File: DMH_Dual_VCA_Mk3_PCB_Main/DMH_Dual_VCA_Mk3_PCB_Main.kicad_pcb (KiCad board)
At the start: 2 copper layers, 49 x 121 mm, 98 parts, among them J10 Conn_01x04, J11 Conn_01x04_PinHeader, J50 Conn_01x08, J60 Conn_01x08, Q5 BC548, Q6 BC548, Q7 BC548, Q8 BC548, SW1 SW_DPDT_OnOffOn_x2, SW2 SW_DPDT_3way, U3 TL074, U4 TL072, U7 TL074, U8 TL074

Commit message: Started Main PCB comp placement
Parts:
- removed C11: 22pF, Capacitor_THT:C_Disc_D3.0mm_W2.0mm_P2.50mm
- removed C12, C13, C14, C15, C16, C17: 100nF, Capacitor_THT:C_Disc_D4.3mm_W1.9mm_P5.00mm
- removed D10, D9: ZPD3V0, Diode_THT:D_DO-35_SOD27_P7.62mm_Horizontal
- removed D5, D6, D7, D8: ZPD4V7, Diode_THT:D_DO-35_SOD27_P7.62mm_Horizontal
- removed J10: Conn_01x04, Connector_PinSocket_2.54mm:PinSocket_1x04_P2.54mm_Vertical
- removed J50, J60: Conn_01x08, Connector_PinSocket_2.54mm:PinSocket_1x08_P2.54mm_Vertical
- removed Q5, Q6, Q7, Q8: BC548, Package_TO_SOT_THT:TO-92L_Inline_Wide
- removed R20: 2k2, Resistor_THT:R_Axial_DIN0207_L6.3mm_D2.5mm_P7.62mm_Horizontal
- removed R21, R40: 18k, Resistor_THT:R_Axial_DIN0207_L6.3mm_D2.5mm_P7.62mm_Horizontal
- removed R27, R29, R37, R50, R51, R52, R53, R54, R55, R56, R64, R65, R66, R67, R69, R70, R71, R72, R74, R75: 100k, Resistor_THT:R_Axial_DIN0207_L6.3mm_D2.5mm_P7.62mm_Horizontal
- removed R43, R47, R57, R63: 100R, Resistor_THT:R_Axial_DIN0207_L6.3mm_D2.5mm_P7.62mm_Horizontal
- removed R44, R46, R58, R60: 20k, Resistor_THT:R_Axial_DIN0207_L6.3mm_D2.5mm_P7.62mm_Horizontal
- removed R45, R48, R49, R59, R61, R62: 10k, Resistor_THT:R_Axial_DIN0207_L6.3mm_D2.5mm_P7.62mm_Horizontal
- removed R68: 33k, Resistor_THT:R_Axial_DIN0207_L6.3mm_D2.5mm_P7.62mm_Horizontal
- removed RV13: 50k, Potentiometer_THT:Potentiometer_Alps_RK09L_Double_Vertical
- removed RV14, RV15: 100k, Potentiometer_THT:Potentiometer_Bourns_3296W_Vertical
- removed RV16: 50k, Potentiometer_THT:Potentiometer_Bourns_3296W_Vertical
- removed RV2, RV3, RV5, RV6: 100k, SynthStuff:Potentiometer_TT_P110KH1
- removed RV4: 100k, SynthStuff:Potentiometer_Alpha_RD901F-40-00D_Single_Vertical
- removed SW1: SW_DPDT_OnOffOn_x2, SynthStuff:Toggle_Switch_2_Poles_TE
- removed SW2: SW_DPDT_3way, SynthStuff:Toggle_Switch_2_Poles_TE
- removed U7, U8: TL074, Package_DIP:DIP-14_W7.62mm_Socket
- added C1: 100nF, Capacitor_THT:C_Disc_D4.3mm_W1.9mm_P5.00mm, B.Cu at (160.8, 77.0)
- added C2: 100nF, Capacitor_THT:C_Disc_D4.3mm_W1.9mm_P5.00mm, B.Cu at (160.8, 80.5)
- added C20: 2.2uF, Capacitor_THT:CP_Radial_D4.0mm_P1.50mm, B.Cu at (139.1, 184.9)
- added C21: 2.2uF, Capacitor_THT:CP_Radial_D4.0mm_P1.50mm, B.Cu at (139.1, 190.4)
- added C22: 22uF, Capacitor_THT:CP_Radial_D4.0mm_P1.50mm, B.Cu at (139.1, 196.0)
- added C23: 22uF, Capacitor_THT:CP_Radial_D4.0mm_P1.50mm, B.Cu at (139.1, 201.6)
- added C24: 100nF, Capacitor_THT:C_Disc_D4.3mm_W1.9mm_P5.00mm, B.Cu at (160.8, 97.8)
- added C25: 100nF, Capacitor_THT:C_Disc_D4.3mm_W1.9mm_P5.00mm, B.Cu at (160.8, 101.2)
- added C3: 22pF, Capacitor_THT:C_Disc_D3.0mm_W2.0mm_P2.50mm, B.Cu at (146.1, 216.5)
- added C4: 47uF, Capacitor_THT:CP_Radial_D5.0mm_P2.00mm, B.Cu at (55.2, 47.0)
- added C5: 47uF, Capacitor_THT:CP_Radial_D5.0mm_P2.00mm, B.Cu at (94.8, 45.0)
- added C6: 100nF, Capacitor_THT:C_Disc_D4.3mm_W1.9mm_P5.00mm, B.Cu at (160.8, 84.0)
- added C9: 100nF, Capacitor_THT:C_Disc_D4.3mm_W1.9mm_P5.00mm, B.Cu at (160.8, 94.3)
- added D1: 1N4148, Diode_THT:D_DO-35_SOD27_P7.62mm_Horizontal, B.Cu at (156.5, 164.5)
- added D13: ZPD3V0, Diode_THT:D_DO-35_SOD27_P7.62mm_Horizontal, B.Cu at (139.6, 160.8)
- added D14: ZPD3V0, Diode_THT:D_DO-35_SOD27_P7.62mm_Horizontal, B.Cu at (139.6, 164.3)
- added D2: 1N4148, Diode_THT:D_DO-35_SOD27_P7.62mm_Horizontal, B.Cu at (156.5, 170.7)
- added J1: TRS_Jack_6.35mm_Sw, SynthStuff:CUI_SJ-63083D, F.Cu at (58.5, 190.2)
- added J100: IDC_02x05, SynthStuff:IDC-Header_2x05_P2.54mm_Vertical_Eurorack, B.Cu at (80.1, 48.8)
- added J12: Conn_01x08, Connector_PinHeader_2.54mm:PinHeader_1x08_P2.54mm_Vertical, F.Cu at (97.2, 138.9)
- added J13: Conn_01x06, Connector_PinHeader_2.54mm:PinHeader_1x06_P2.54mm_Vertical, F.Cu at (52.8, 52.0)
- added J18: Conn_02x03_Odd_Even, Connector_PinSocket_2.54mm:PinSocket_2x03_P2.54mm_Vertical, B.Cu at (171.2, 114.4)
- added J19: Conn_02x03_Odd_Even, Connector_PinSocket_2.54mm:PinSocket_2x03_P2.54mm_Vertical, B.Cu at (171.2, 124.1)
- added J2: TRS_Jack_6.35mm_Sw, SynthStuff:CUI_SJ-63083D, F.Cu at (75.0, 190.2)
- added J20: Conn_01x01, Connector_PinHeader_2.54mm:PinHeader_1x01_P2.54mm_Vertical, B.Cu at (40.2, 46.2)
- added J200: IDC_02x05, SynthStuff:IDC-Header_2x05_P2.54mm_Vertical_BackBone, B.Cu at (71.4, 157.2)
- added J21: Conn_01x08, Connector_PinHeader_2.54mm:PinHeader_1x08_P2.54mm_Vertical, F.Cu at (97.2, 52.0)
- added J22: Conn_02x03_Odd_Even, Connector_PinSocket_2.54mm:PinSocket_2x03_P2.54mm_Vertical, B.Cu at (171.2, 133.8)
- added J23: Conn_02x03_Odd_Even, Connector_PinSocket_2.54mm:PinSocket_2x03_P2.54mm_Vertical, B.Cu at (171.2, 143.5)
- added J3: TRS_Jack_6.35mm_Sw, SynthStuff:CUI_SJ-63083D, F.Cu at (58.5, 171.8)
- added J4: TRS_Jack_6.35mm_Sw, SynthStuff:CUI_SJ-63083D, F.Cu at (91.5, 190.2)
- added J5: TRS_Jack_6.35mm_Sw, SynthStuff:CUI_SJ-63083D, F.Cu at (58.5, 208.8)
- added J6: TRS_Jack_6.35mm_Sw, SynthStuff:CUI_SJ-63083D, F.Cu at (75.0, 208.8)
- added J7: TRS_Jack_6.35mm_Sw, SynthStuff:CUI_SJ-63083D, F.Cu at (75.0, 171.8)
- added J8: TRS_Jack_6.35mm_Sw, SynthStuff:CUI_SJ-63083D, F.Cu at (91.5, 208.8)
- added J9: TRS_Jack_6.35mm_Sw, SynthStuff:CUI_SJ-63083D, F.Cu at (91.5, 171.8)
- added JP1: Jumper, Connector_PinHeader_2.54mm:PinHeader_1x03_P2.54mm_Vertical, B.Cu at (90.5, 160.5)
- added Q10: BC548, Package_TO_SOT_THT:TO-92_Inline, B.Cu at (150.3, 191.2)
- added Q11: BC548, Package_TO_SOT_THT:TO-92_Inline, B.Cu at (150.3, 197.0)
- added Q12: BC548, Package_TO_SOT_THT:TO-92_Inline, B.Cu at (150.3, 202.8)
- added Q9: BC548, Package_TO_SOT_THT:TO-92_Inline, B.Cu at (150.3, 185.4)
- added R1: 3k3, Resistor_THT:R_Axial_DIN0207_L6.3mm_D2.5mm_P7.62mm_Horizontal, B.Cu at (151.8, 77.3)
- added R10: 10k, Resistor_THT:R_Axial_DIN0207_L6.3mm_D2.5mm_P7.62mm_Horizontal, B.Cu at (151.8, 113.8)
- added R100: 1k, Resistor_THT:R_Axial_DIN0207_L6.3mm_D2.5mm_P7.62mm_Horizontal, B.Cu at (118.1, 101.6)
- added R101: 1k, Resistor_THT:R_Axial_DIN0207_L6.3mm_D2.5mm_P7.62mm_Horizontal, B.Cu at (118.1, 105.7)
- added R11: 20k, Resistor_THT:R_Axial_DIN0207_L6.3mm_D2.5mm_P7.62mm_Horizontal, B.Cu at (151.8, 117.8)
- added R12: 100k, Resistor_THT:R_Axial_DIN0207_L6.3mm_D2.5mm_P7.62mm_Horizontal, B.Cu at (151.8, 121.9)
- added R13: 100k, Resistor_THT:R_Axial_DIN0207_L6.3mm_D2.5mm_P7.62mm_Horizontal, B.Cu at (151.8, 125.9)
- added R14: 100k, Resistor_THT:R_Axial_DIN0207_L6.3mm_D2.5mm_P7.62mm_Horizontal, B.Cu at (151.8, 130.0)
- added R15: 100k, Resistor_THT:R_Axial_DIN0207_L6.3mm_D2.5mm_P7.62mm_Horizontal, B.Cu at (151.8, 134.0)
- added R2: 3k3, Resistor_THT:R_Axial_DIN0207_L6.3mm_D2.5mm_P7.62mm_Horizontal, B.Cu at (151.8, 81.4)
- added R3: 33k, Resistor_THT:R_Axial_DIN0207_L6.3mm_D2.5mm_P7.62mm_Horizontal, B.Cu at (151.8, 85.4)
- added R4: 100k, Resistor_THT:R_Axial_DIN0207_L6.3mm_D2.5mm_P7.62mm_Horizontal, B.Cu at (151.8, 89.5)
- added R6: 100k, Resistor_THT:R_Axial_DIN0207_L6.3mm_D2.5mm_P7.62mm_Horizontal, B.Cu at (151.8, 97.6)
- added R7: 100k, Resistor_THT:R_Axial_DIN0207_L6.3mm_D2.5mm_P7.62mm_Horizontal, B.Cu at (151.8, 101.6)
- added R8: 100k, Resistor_THT:R_Axial_DIN0207_L6.3mm_D2.5mm_P7.62mm_Horizontal, B.Cu at (151.8, 105.7)
- added R9: 20k, Resistor_THT:R_Axial_DIN0207_L6.3mm_D2.5mm_P7.62mm_Horizontal, B.Cu at (151.8, 109.7)
- added R92: 100k, Resistor_THT:R_Axial_DIN0207_L6.3mm_D2.5mm_P7.62mm_Horizontal, B.Cu at (128.9, 105.7)
- added R93: 100k, Resistor_THT:R_Axial_DIN0207_L6.3mm_D2.5mm_P7.62mm_Horizontal, B.Cu at (128.9, 109.7)
- added R94: 220k, Resistor_THT:R_Axial_DIN0207_L6.3mm_D2.5mm_P7.62mm_Horizontal, B.Cu at (118.1, 77.3)
- added R95: 220k, Resistor_THT:R_Axial_DIN0207_L6.3mm_D2.5mm_P7.62mm_Horizontal, B.Cu at (118.1, 81.3)
- added R96: 100k, Resistor_THT:R_Axial_DIN0207_L6.3mm_D2.5mm_P7.62mm_Horizontal, B.Cu at (118.1, 85.4)
- added R97: 100k, Resistor_THT:R_Axial_DIN0207_L6.3mm_D2.5mm_P7.62mm_Horizontal, B.Cu at (118.1, 89.5)
- added R98: 2k2, Resistor_THT:R_Axial_DIN0207_L6.3mm_D2.5mm_P7.62mm_Horizontal, B.Cu at (118.1, 93.5)
- added R99: 2k2, Resistor_THT:R_Axial_DIN0207_L6.3mm_D2.5mm_P7.62mm_Horizontal, B.Cu at (118.1, 97.5)
- added U1: LM4040LP-5, Package_TO_SOT_THT:TO-92_Inline, B.Cu at (155.6, 148.2)
- added U10: TL074, Package_DIP:DIP-14_W7.62mm_Socket, B.Cu at (121.7, 126.7)
- added U2: LM4040LP-5, Package_TO_SOT_THT:TO-92_Inline, B.Cu at (155.6, 156.4)
- C7, C8, D11, D12, R5, R80, R81, R83, R87, U3, U4: moved to B.Cu
- D3, D4: value 1N4148 -> SB140; footprint Diode_THT:D_DO-35_SOD27_P7.62mm_Horizontal -> Diode_THT:D_DO-41_SOD81_P10.16mm_Horizontal; moved to B.Cu
- J11: value Conn_01x04_PinHeader -> Conn_01x06; footprint Connector_PinSocket_2.54mm:PinSocket_1x04_P2.54mm_Vertical -> Connector_PinHeader_2.54mm:PinHeader_1x06_P2.54mm_Vertical
- R76: value 100k -> 10k; moved to B.Cu
- R77: value 20k -> 1k5; moved to B.Cu
- R78: value 20k -> 10k; moved to B.Cu
- R79: value 10k -> 1k5; moved to B.Cu
- R82: value 220k -> 100k; moved to B.Cu
- R84: value 2k2 -> 100k; moved to B.Cu
- R85: value 100k -> 4k7; moved to B.Cu
- R86: value 220k -> 1k; moved to B.Cu
- R88: value 2k2 -> 4k7; moved to B.Cu
- R89: value 2k2 -> 1k; moved to B.Cu
- R90, R91: value 1k -> 2k2; moved to B.Cu
- RV1: value 100k -> 50k; footprint SynthStuff:Potentiometer_Alpha_RD901F-40-00D_Single_Vertical -> Potentiometer_THT:Potentiometer_Bourns_3296W_Vertical; moved to B.Cu
- moved J11 179.2 mm to (52.8, 144.0)
- moved RV1 174.3 mm to (142.2, 228.0), turned to 180 degrees
- moved D4 151.9 mm to (61.2, 54.6), turned to 90 degrees
- moved D3 136.0 mm to (88.8, 44.4), turned to -90 degrees
- moved R85 81.8 mm to (128.9, 77.3), turned to 180 degrees
- moved R86 81.8 mm to (128.9, 81.3), turned to 180 degrees
- moved R87 81.8 mm to (128.9, 85.4), turned to 180 degrees
- moved R88 81.8 mm to (128.9, 89.5), turned to 180 degrees
- moved R89 81.8 mm to (128.9, 93.5), turned to 180 degrees
- moved R90 81.8 mm to (128.9, 97.5), turned to 180 degrees
- moved R91 81.8 mm to (128.9, 101.6), turned to 180 degrees
- moved D11 81.0 mm to (139.6, 153.7), turned to 180 degrees
- moved D12 81.0 mm to (139.6, 157.2), turned to 180 degrees
- moved C7 68.8 mm to (160.8, 87.4), turned to 180 degrees
- moved C8 68.8 mm to (160.8, 90.8), turned to 180 degrees
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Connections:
- C7 pad 1: +12V -> GND
- C7 pad 2: GND -> -12V
- C8 pad 1: GND -> +12V
- C8 pad 2: -12V -> GND
- D11 pad 1: Net-(D11-K) -> /Clipping/Clip_Sw_p1_m
- D3 pad 2: Net-(D3-A) -> -12V
- D4 pad 1: Net-(D4-K) -> +12V
- D4 pad 2: Net-(D3-K) -> Net-(D4-A)
- J11 pad 1: /2nd VCA/Input A -> /Processed_CV_A_m
- J11 pad 2: /Clipping/Output A -> /Processed_CV_B_m
- J11 pad 3: /Clipping/Output B -> /CV_In_A1_m
- J11 pad 4: /2nd VCA/Input B -> /CV_In_A2_m
- R5 pad 1: /2nd VCA/CV PT Offset -> Net-(D2-K)
- R5 pad 2: Net-(U3A--) -> GND
- R76 pad 1: Net-(D4-K) -> Net-(Q9-B)
- R76 pad 2: GND -> Net-(C20-Pad2)
- R77 pad 1: Net-(U7C--) -> -12V
- R77 pad 2: Net-(R75-Pad1) -> Net-(Q9-B)
- R78 pad 1: /2nd VCA/Balanced Offset -> Net-(Q10-B)
- R78 pad 2: Net-(U7C--) -> Net-(C21-Pad2)
- R79 pad 1: -5V -> -12V
- R79 pad 2: Net-(U7C--) -> Net-(Q10-B)
- R80 pad 1: Net-(U8B--) -> /Clip_In_A_m
- R80 pad 2: Net-(R80-Pad2) -> Net-(U10A--)
- R81 pad 1: Net-(SW1A-B) -> /Clip_In_B_m
- R81 pad 2: Net-(U8B--) -> Net-(U10D--)
- R82 pad 2: Net-(U8B--) -> +12V
- R83 pad 1: Net-(R83-Pad1) -> Net-(Q10-C)
- R83 pad 2: Net-(U8D--) -> +12V
- R84 pad 1: Net-(R83-Pad1) -> Net-(R84-Pad1)
- R84 pad 2: Net-(SW1B-B) -> Net-(U10A--)
- R85 pad 1: Net-(SW1B-B) -> /Clipping/LED_A_pA_m
- R85 pad 2: Net-(U8C--) -> +12V
- R86 pad 1: Net-(D11-K) -> -12V
- R86 pad 2: Net-(U8C--) -> /Clipping/LED_A_pK_m
- R87 pad 1: Net-(U8C--) -> Net-(R87-Pad1)
- R87 pad 2: Net-(R87-Pad2) -> Net-(U10D--)
- R88 pad 1: Net-(R80-Pad2) -> /Clipping/LED_B_pA_m
- R88 pad 2: Net-(R88-Pad2) -> +12V
- R89 pad 1: Net-(R87-Pad2) -> -12V
- R89 pad 2: Net-(R89-Pad2) -> /Clipping/LED_B_pK_m
- R90 pad 1: Net-(R88-Pad2) -> Net-(R84-Pad1)
- R90 pad 2: /Clipping/Output A -> /Clipping/Clip_Sw_p2_m
- R91 pad 1: Net-(R89-Pad2) -> Net-(R87-Pad1)
- R91 pad 2: /Clipping/Output B -> /Clipping/Clip_Sw_p5_m
- RV1 pad 1: GND -> Net-(U4A--)
- RV1 pad 2: /Inputs and Outputs/Offset A Pot -> /Attenuverted_CV_PT_m
- RV1 pad 3: Net-(R21-Pad1) -> /Attenuverted_CV_PT_m
- U3 pad 10: Net-(U3C-+) -> GND
- U3 pad 14: Net-(R45-Pad1) -> Net-(U3D--)
- U3 pad 2: Net-(U3A--) -> Net-(D1-A)
- U3 pad 3: GND -> /CV_PT_Pot_G2_m
- U3 pad 5: Net-(U3B-+) -> Net-(D2-K)
- U3 pad 7: /2nd VCA/Output B -> Net-(R7-Pad1)
- U3 pad 8: /2nd VCA/Output A -> /Balanced_Offset_m
- U4 pad 1: /2nd VCA/Attenuverted CV PT -> /Attenuverted_CV_PT_m
- U4 pad 3: /2nd VCA/CV PT Pot G1 -> /CV_PT_Pot_G1_m
- U4 pad 7: /2nd VCA/Inverted CV PT -> /Inverted_CV_PT_m
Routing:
- added copper zone on B.Cu, net GND
- added copper zone on F.Cu, net GND
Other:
- board size 49 x 121 mm -> 49 x 175 mm
- board text added: "Mk3.0 June 2026"
- board text removed: "Mk2.0 - October 2025"

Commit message: Comp placement in progress
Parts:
- moved J22 101.5 mm to (73.0, 108.0), turned to 90 degrees
- moved J19 101.0 mm to (73.0, 147.6), turned to 90 degrees
- moved J23 100.7 mm to (73.0, 121.2), turned to 90 degrees
- moved J18 100.2 mm to (73.0, 134.4), turned to 90 degrees
- moved U3 95.3 mm to (68.5, 83.8)
- moved C8 94.2 mm to (67.2, 80.6)
- moved C9 93.8 mm to (67.4, 102.7)
- moved C24 91.9 mm to (77.5, 59.1)
- moved C25 85.8 mm to (77.5, 80.9)
- moved U10 77.3 mm to (78.8, 62.4)
- moved U4 65.8 mm to (89.3, 91.5)
- moved R100 6.50 mm to (111.6, 101.8)
- moved J200 1.50 mm to (69.9, 157.3)
- moved JP1 1.50 mm to (89.0, 160.6)
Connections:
- J200 pad 1: /Input_A_N_m -> /CV_In_A2_N_m
- J200 pad 3: /CV_In_A1_N_m -> /CV_In_B2_N_m
- J200 pad 6: /CV_In_A2_N_m -> /Input_A_N_m
- J200 pad 8: /CV_In_B2_N_m -> /CV_In_A1_N_m

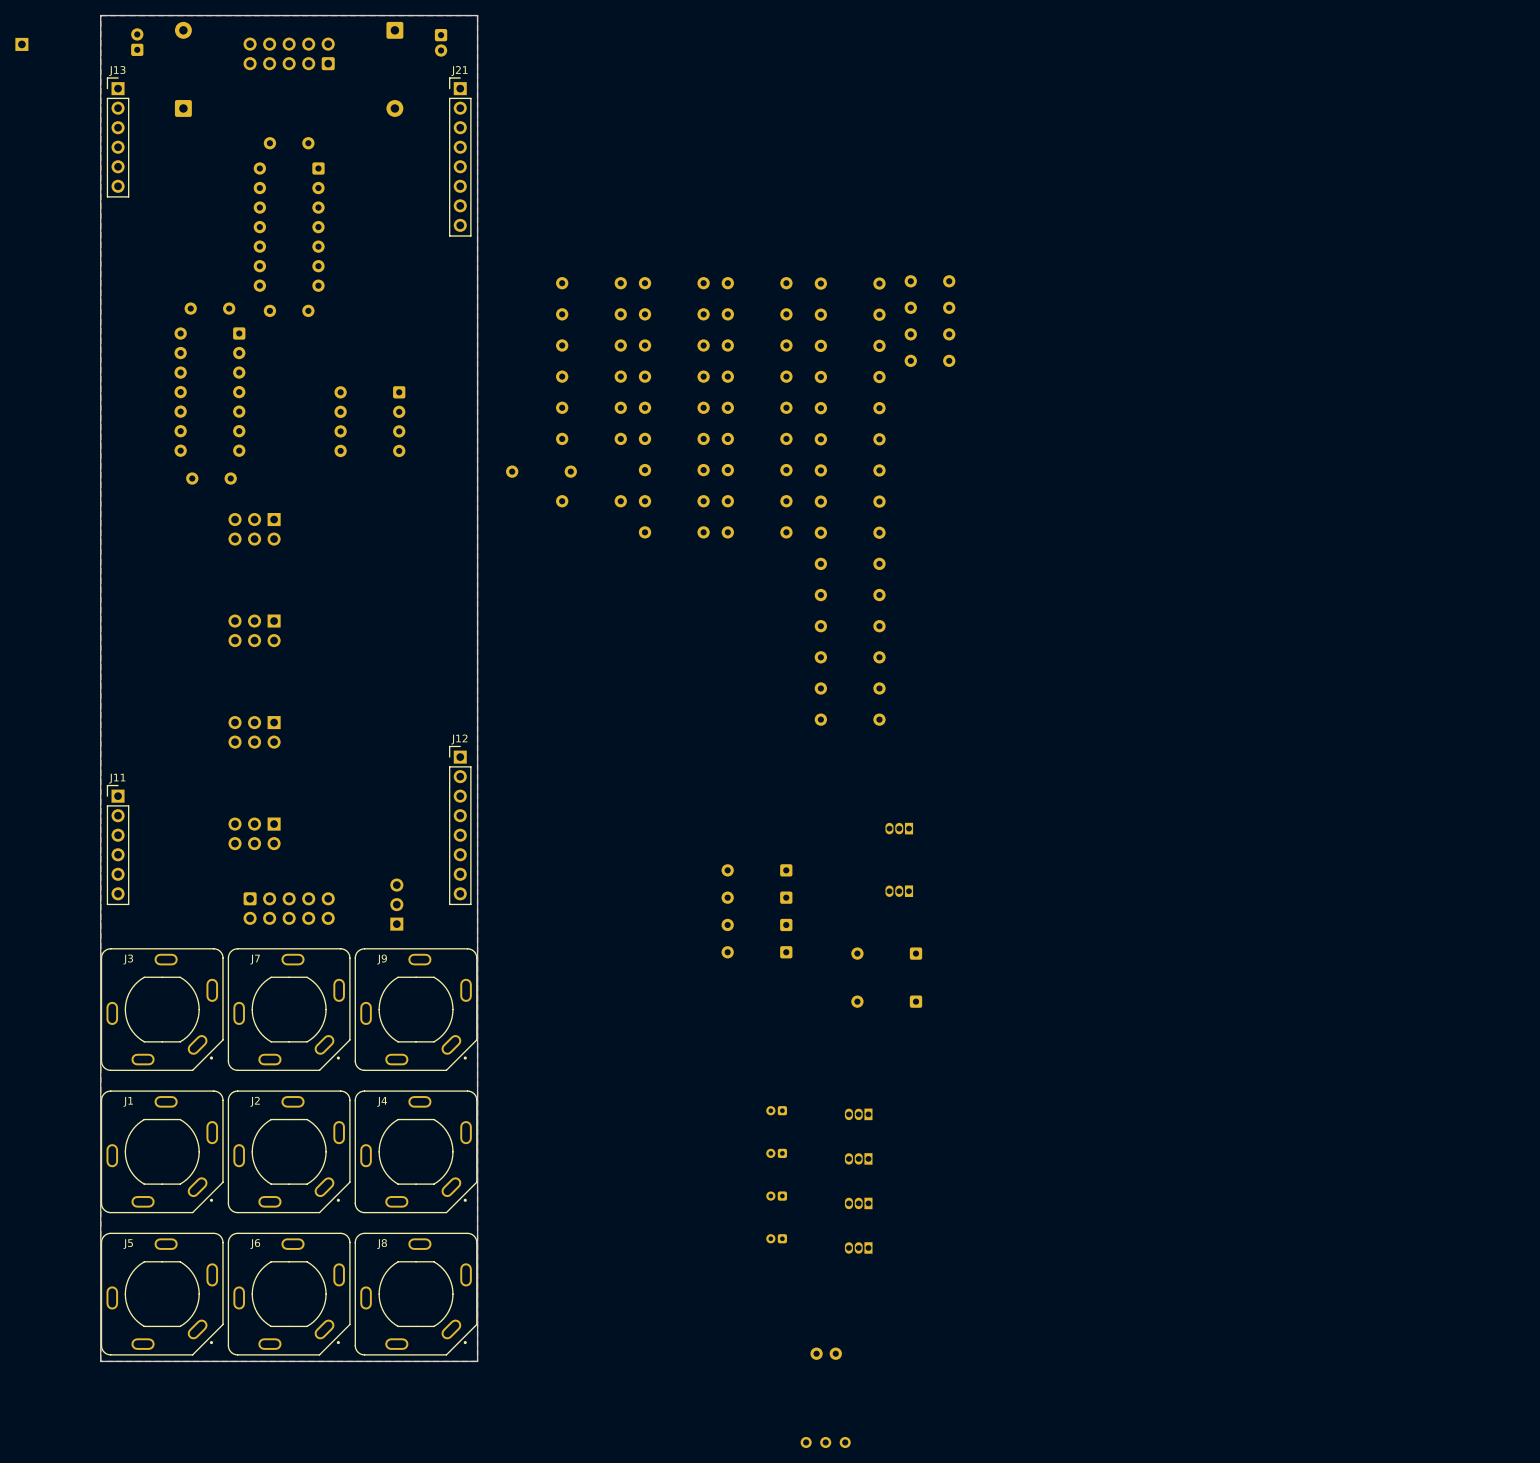
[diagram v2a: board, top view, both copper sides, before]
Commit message: Main comp placement in progress
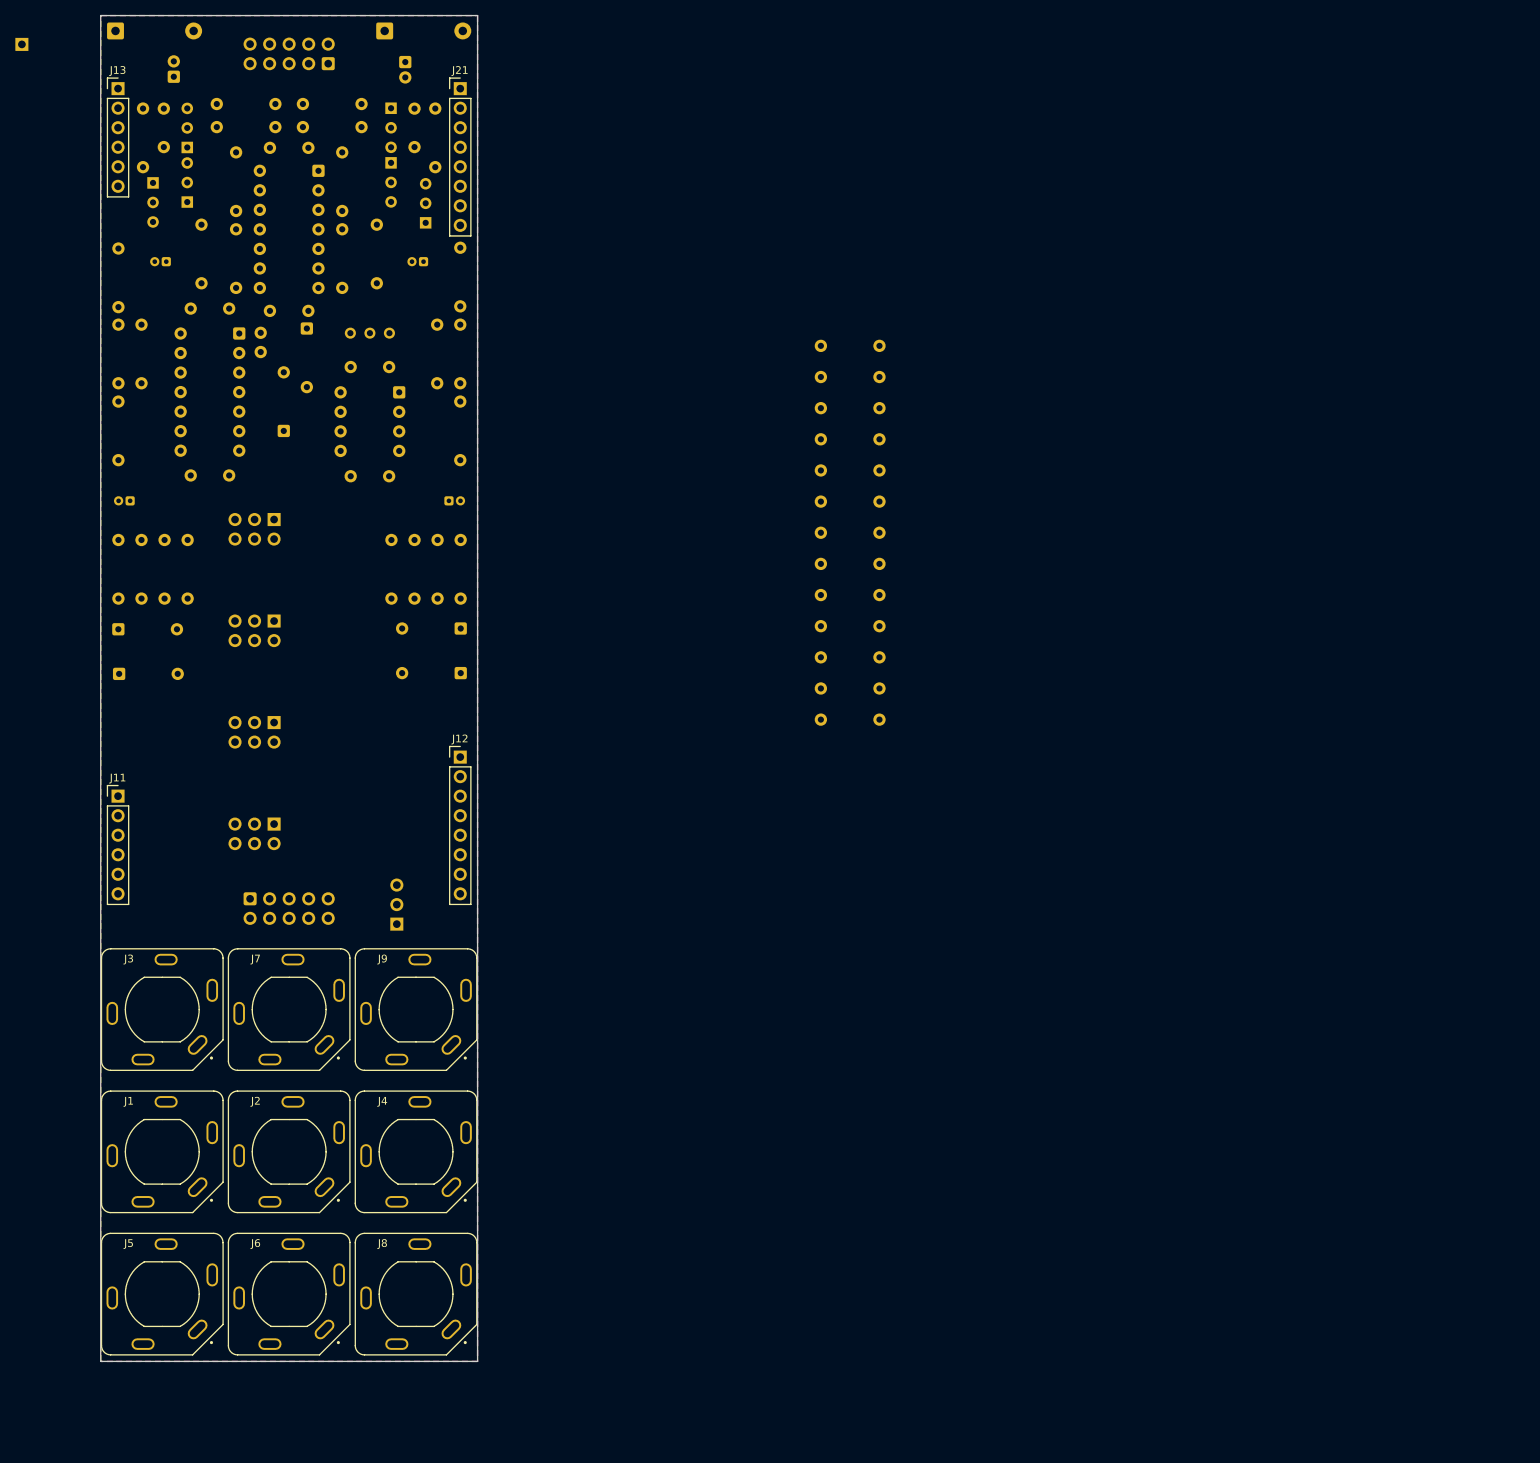
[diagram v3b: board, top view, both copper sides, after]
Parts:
- Q10, Q11, Q12, Q9, U1, U2: footprint Package_TO_SOT_THT:TO-92_Inline -> Package_TO_SOT_THT:TO-92L_Inline_Wide
- moved Q12 162.3 mm to (61.8, 66.8), turned to 90 degrees
- moved Q10 157.4 mm to (57.3, 64.3), turned to -90 degrees
- moved RV1 155.9 mm to (83.0, 83.8)
- moved C3 152.4 mm to (71.3, 83.8), turned to -90 degrees
- moved C23 150.2 mm to (59.0, 74.5)
- moved Q11 139.9 mm to (92.8, 69.5), turned to 90 degrees
- moved Q9 138.4 mm to (88.2, 61.6), turned to -90 degrees
- moved C22 130.2 mm to (92.5, 74.5)
- moved U1 129.0 mm to (61.8, 59.6), turned to 90 degrees
- moved U2 122.1 mm to (88.2, 54.5), turned to -90 degrees
- moved C21 120.0 mm to (54.3, 105.6)
- moved D1 113.5 mm to (77.3, 83.2), turned to -90 degrees
- moved D2 110.8 mm to (74.3, 96.5), turned to 90 degrees
- moved C1 104.6 mm to (58.7, 54.6), turned to -90 degrees
- moved R1 98.4 mm to (56.0, 54.6), turned to -90 degrees
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
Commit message: Main comp placement done
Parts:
- moved R10 104.4 mm to (55.8, 72.8), turned to -90 degrees
- moved R11 97.2 mm to (55.9, 101.9), turned to 90 degrees
- moved R9 91.0 mm to (60.9, 104.7), turned to 0 degrees
- moved J20 90.7 mm to (52.9, 136.1)
- moved R4 80.3 mm to (71.6, 94.0), turned to 90 degrees
- moved R5 80.2 mm to (71.6, 96.2), turned to -90 degrees
- moved R7 77.2 mm to (74.6, 103.8), turned to 90 degrees
- moved R8 73.3 mm to (78.6, 101.7), turned to 90 degrees
- moved R15 66.7 mm to (85.7, 143.7)
- moved R14 66.6 mm to (85.7, 138.8)
- moved R13 66.5 mm to (85.7, 133.9)
- moved R12 66.5 mm to (85.7, 128.9)
- moved R6 62.9 mm to (89.4, 105.6)
- moved R3 59.9 mm to (94.2, 101.9), turned to 90 degrees
- moved C3 3.00 mm to (71.3, 80.8)
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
